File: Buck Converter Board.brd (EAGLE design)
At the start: 160 x 100 mm, 6 parts, among them J1 POWERPOLE_POWER25A_HORIZONTAL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, J2 POWERPOLE_POWER25A_HORIZONTAL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

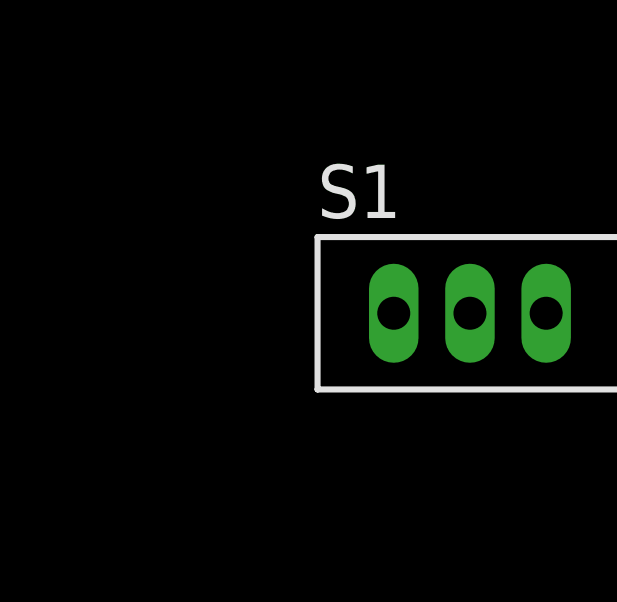
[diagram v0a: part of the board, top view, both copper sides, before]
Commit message: moved cmoponents on buck converter board around
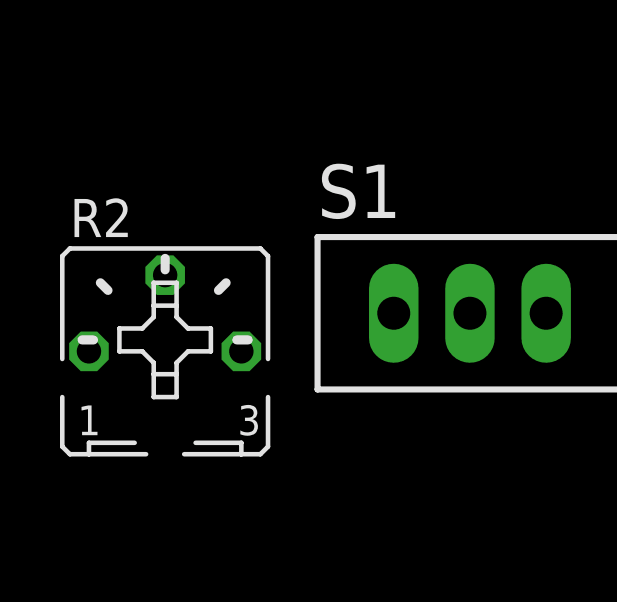
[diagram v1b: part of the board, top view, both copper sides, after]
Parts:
- added R2: (no value), pot:B25P
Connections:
- new net N$10: R2.E
- new net N$7: R2.S
- new net N$9: R2.A
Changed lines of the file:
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@@
 </element>
 <element name="S1" library="switch" library_urn="urn:adsk.eagle:library:380" package="TL3XPO" package3d_urn="urn:adsk.eagle:package:27745/1" value="TL38PO" x="-85.09" y="7.62"/>
+<element name="R2" library="pot" library_urn="urn:adsk.eagle:library:331" package="B25P" package3d_urn="urn:adsk.eagle:package:22684/1" value="" x="-95.25" y="6.35"/>
 </elements>
 <signals>
@@
 <wire x1="5.83" y1="46.85" x2="-85.09" y2="7.62" width="0" layer="19" extent="1-1"/>
 </signal>
-<signal name="N$4">
-<contactref element="R1" pad="1"/>
-</signal>
 <signal name="N$5">
-<contactref element="R1" pad="2"/>
 <contactref element="C1" pad="1"/>
 <contactref element="J2" pad="RED"/>
+<contactref element="R1" pad="2"/>
+<wire x1="144.46" y1="52.07" x2="147.46" y2="72.91" width="0" layer="19" extent="1-1"/>
 <wire x1="137.48" y1="52.07" x2="144.46" y2="52.07" width="0" layer="19" extent="1-1"/>
-<wire x1="147.46" y1="72.91" x2="144.46" y2="52.07" width="0" layer="19" extent="1-1"/>
 </signal>
 <signal name="N$6">
@@
 <contactref element="S1" pad="1"/>
 </signal>
+<signal name="N$4">
+<contactref element="R1" pad="1"/>
+</signal>
+<signal name="N$7">
+<contactref element="R2" pad="S"/>
+</signal>
+<signal name="N$9">
+<contactref element="R2" pad="A"/>
+</signal>
+<signal name="N$10">
+<contactref element="R2" pad="E"/>
+</signal>
 </signals>

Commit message: removed trim pot and bullshit from buck board
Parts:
- removed R1: (no value), rcl:R0805
- removed R2: (no value), pot:B25P
- removed S1: TL38PO, switch:TL3XPO
- added D1: (no value), diode:SMB
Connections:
- removed net N$10: R2.E
- removed net N$7: R2.S
- removed net N$8: S1.1
- removed net N$9: R2.A
- new net N$11: D1.C
- new net N$12: D1.A
- net N$3: no longer S1.2
- net N$4: now also J2.RED; no longer R1.1
- net N$5: no longer J2.RED, R1.2
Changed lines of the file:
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@@
 <layer number="97" name="Info" color="7" fill="1" visible="no" active="no"/>
 <layer number="98" name="Guide" color="6" fill="1" visible="no" active="no"/>
+<layer number="99" name="SpiceOrder" color="5" fill="1" visible="no" active="no"/>
 </layers>
 <board>
@@
 <element name="J1" library="powerpoles" package="POWERPOLE_PAIR_25A_HORIZ_G2" value="POWERPOLE_POWER25A_HORIZONTAL_G2" x="-1.27" y="50.8" rot="R90"/>
 <element name="J2" library="powerpoles" package="POWERPOLE_PAIR_25A_HORIZ_G2" value="POWERPOLE_POWER25A_HORIZONTAL_G2" x="143.51" y="80.01"/>
-<element name="R1" library="rcl" library_urn="urn:adsk.eagle:library:334" package="R0805" package3d_urn="urn:adsk.eagle:package:23553/2" value="" x="143.51" y="52.07">
-<attribute name="SPICEPREFIX" value="R" x="143.51" y="52.07" size="1.778" layer="27" display="off"/>
-</element>
-<element name="S1" library="switch" library_urn="urn:adsk.eagle:library:380" package="TL3XPO" package3d_urn="urn:adsk.eagle:package:27745/1" value="TL38PO" x="-85.09" y="7.62"/>
-<element name="R2" library="pot" library_urn="urn:adsk.eagle:library:331" package="B25P" package3d_urn="urn:adsk.eagle:package:22684/1" value="" x="-95.25" y="6.35"/>
+<element name="D1" library="diode" library_urn="urn:adsk.eagle:library:210" package="SMB" package3d_urn="urn:adsk.eagle:package:43404/2" value="" x="59.69" y="73.66"/>
 </elements>
 <signals>
@@
 <signal name="N$3">
 <contactref element="J1" pad="BLACK"/>
-<contactref element="S1" pad="2"/>
-<wire x1="5.83" y1="46.85" x2="-85.09" y2="7.62" width="0" layer="19" extent="1-1"/>
-</signal>
-<signal name="N$5">
-<contactref element="C1" pad="1"/>
-<contactref element="J2" pad="RED"/>
-<contactref element="R1" pad="2"/>
-<wire x1="144.46" y1="52.07" x2="147.46" y2="72.91" width="0" layer="19" extent="1-1"/>
-<wire x1="137.48" y1="52.07" x2="144.46" y2="52.07" width="0" layer="19" extent="1-1"/>
 </signal>
 <signal name="N$6">
@@
 <wire x1="139.38" y1="52.07" x2="139.56" y2="72.91" width="0" layer="19" extent="1-1"/>
 </signal>
-<signal name="N$8">
-<contactref element="S1" pad="1"/>
-</signal>
 <signal name="N$4">
-<contactref element="R1" pad="1"/>
-</signal>
-<signal name="N$7">
-<contactref element="R2" pad="S"/>
-</signal>
-<signal name="N$9">
-<contactref element="R2" pad="A"/>
-</signal>
-<signal name="N$10">
-<contactref element="R2" pad="E"/>
+<contactref element="J2" pad="RED"/>
+</signal>
+<signal name="N$5">
+<contactref element="C1" pad="1"/>
+</signal>
+<signal name="N$11">
+<contactref element="D1" pad="C"/>
+</signal>
+<signal name="N$12">
+<contactref element="D1" pad="A"/>
 </signal>
 </signals>
